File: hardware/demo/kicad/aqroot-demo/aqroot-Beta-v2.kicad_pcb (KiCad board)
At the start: 6 copper layers, 72 x 148 mm, 311 parts, among them J1 FH69-50S-0.5SH, J2 Molex_5025700893, J3 USB_C_Receptacle_USB2.0_16P, J4 JST-PH-2 BATTERY, J5 COMMUNITY_PORT_1x24, J6 JST-PH-2 SPEAKER, J7 BM02B-ACHSS-GAN-ETF, J8 QWIIC_STEMMA_QT, Q1 AO3400A, Q10 2N7002, Q2 NTMD4820N, Q3 NTMD4820N, Q4 BSS138, Q5 AO3401A, Q6 BSS138, Q7 BSS138, Q8 BSS138, Q9 BSS138, SW1 BOOT, SW2 UP, SW3 DOWN, SW4 LEFT, SW5 RIGHT, SW6 A_SELECT, SW7 B_BACK, SW9 SW_SPDT, U1 ESP32-S3-WROOM-1, U10 USBLC6-2SC6, U11 BQ25185, U12 TPS63020, U13 TPS61023, U14 MAX17048, U16 TCA4307DGKR, U17 TPS61169DCKR, U18 LTC4368-1, U19 TLV7032, U2 PCAL9535APW, U20 TPS22950C, U21 TPS61023, U22 TPS22950C, U3 PCAL9535APW, U4 BMI270, U5 MAX98357A, U6 TSOP38238, U7 E07-400M10S, U8 E22-900M22S, U9 ST25R3916-AQET, Y1 27.12MHz 10pF 3225-4P

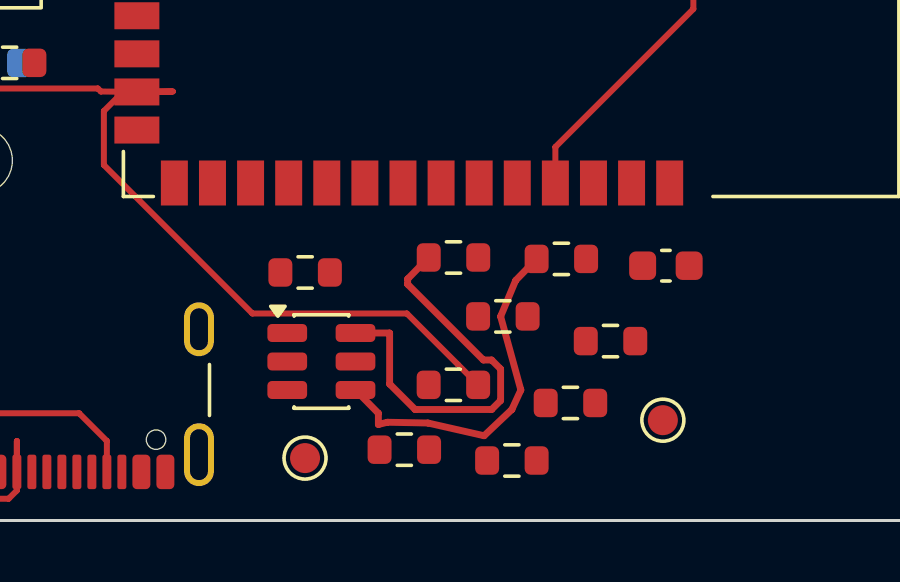
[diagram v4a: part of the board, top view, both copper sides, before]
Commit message: demo: route native A internal leg
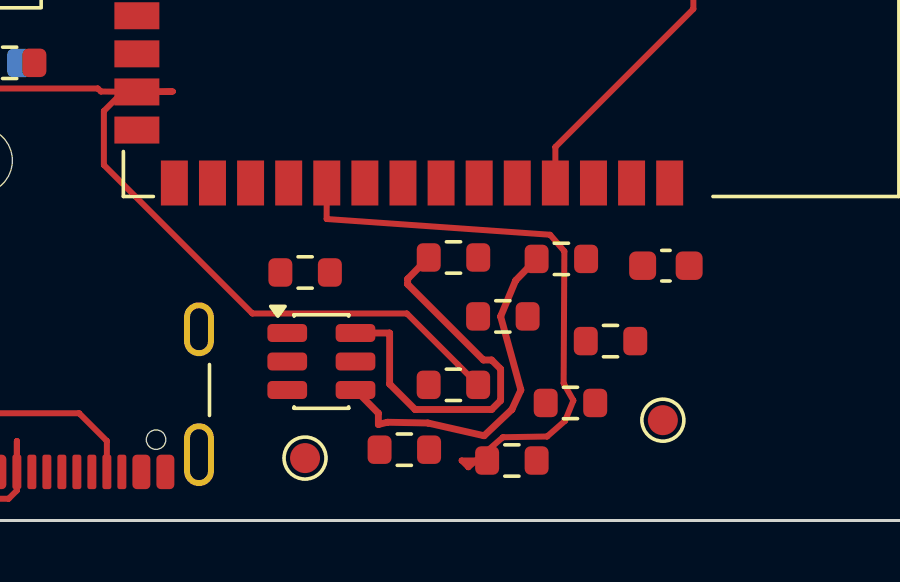
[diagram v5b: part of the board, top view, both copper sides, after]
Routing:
- net /NATIVE_A: track 0.00 -> 20.1 mm
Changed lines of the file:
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@@
+	)
+	(segment
+		(start 59.8 144)
+		(end 59.525 144.675)
+		(width 0.2)
+		(layer "F.Cu")
+		(net "/NATIVE_A")
+	)
+	(segment
+		(start 59.5 139.025)
+		(end 59.475 143.425)
+		(width 0.2)
+		(layer "F.Cu")
+		(net "/NATIVE_A")
+	)
+	(segment
+		(start 59.525 144.675)
+		(end 58.925 145.2)
+		(width 0.2)
+		(layer "F.Cu")
+		(net "/NATIVE_A")
+	)
+	(segment
+		(start 51.58 136.75)
+		(end 51.575 137.95)
+		(width 0.2)
+		(layer "F.Cu")
+		(net "/NATIVE_A")
+	)
+	(segment
+		(start 57.45 145.225)
+		(end 56.3 146.225)
+		(width 0.2)
+		(layer "F.Cu")
+		(net "/NATIVE_A")
+	)
+	(segment
+		(start 58.925 145.2)
+		(end 57.45 145.225)
+		(width 0.2)
+		(layer "F.Cu")
+		(net "/NATIVE_A")
+	)
+	(segment
+		(start 59.025 138.475)
+		(end 59.5 139.025)
+		(width 0.2)
+		(layer "F.Cu")
+		(net "/NATIVE_A")
+	)
+	(segment
+		(start 51.575 137.95)
+		(end 59.025 138.475)
+		(width 0.2)
+		(layer "F.Cu")
+		(net "/NATIVE_A")
+	)
+	(segment
+		(start 56.925 146)
+		(end 56.075 146)
+		(width 0.2)
+		(layer "F.Cu")
+		(net "/NATIVE_A")
+	)
+	(segment
+		(start 59.475 143.425)
+		(end 59.8 144)
+		(width 0.2)
+		(layer "F.Cu")
+		(net "/NATIVE_A")
+	)
+	(segment
+		(start 56.3 146.225)
+		(end 56.075 146)
+		(width 0.2)
+		(layer "F.Cu")
+		(net "/NATIVE_A")
 	)
 	(segment

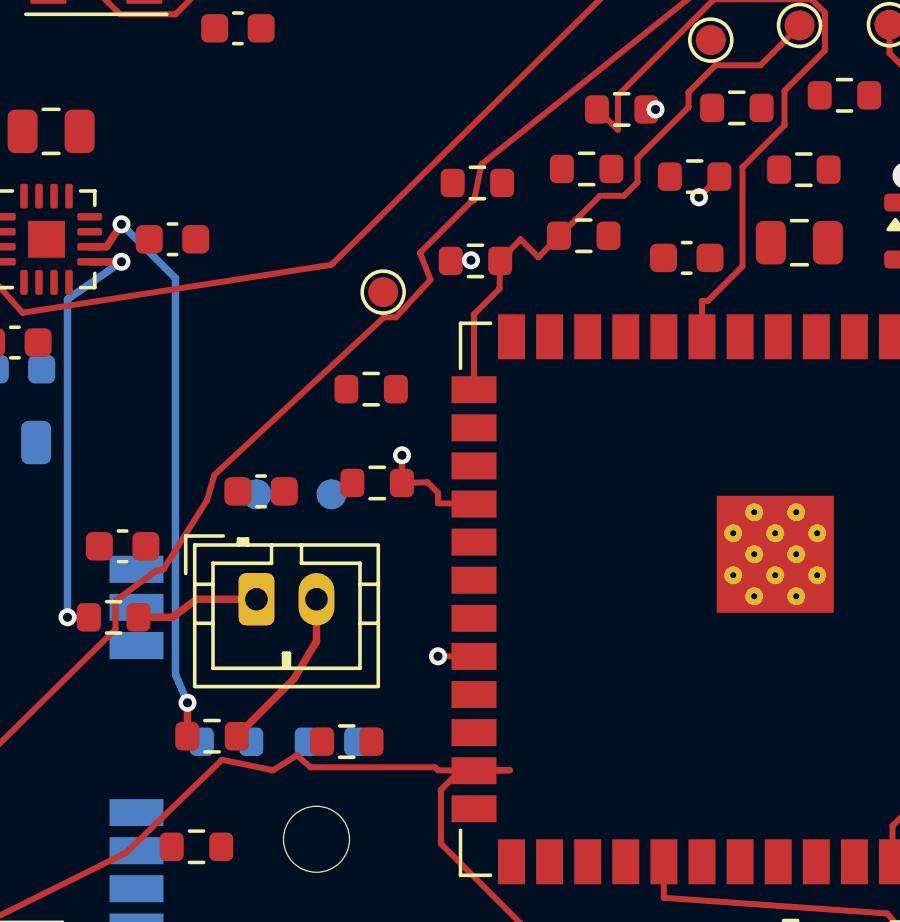
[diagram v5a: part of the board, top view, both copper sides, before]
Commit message: demo: route native B internal leg
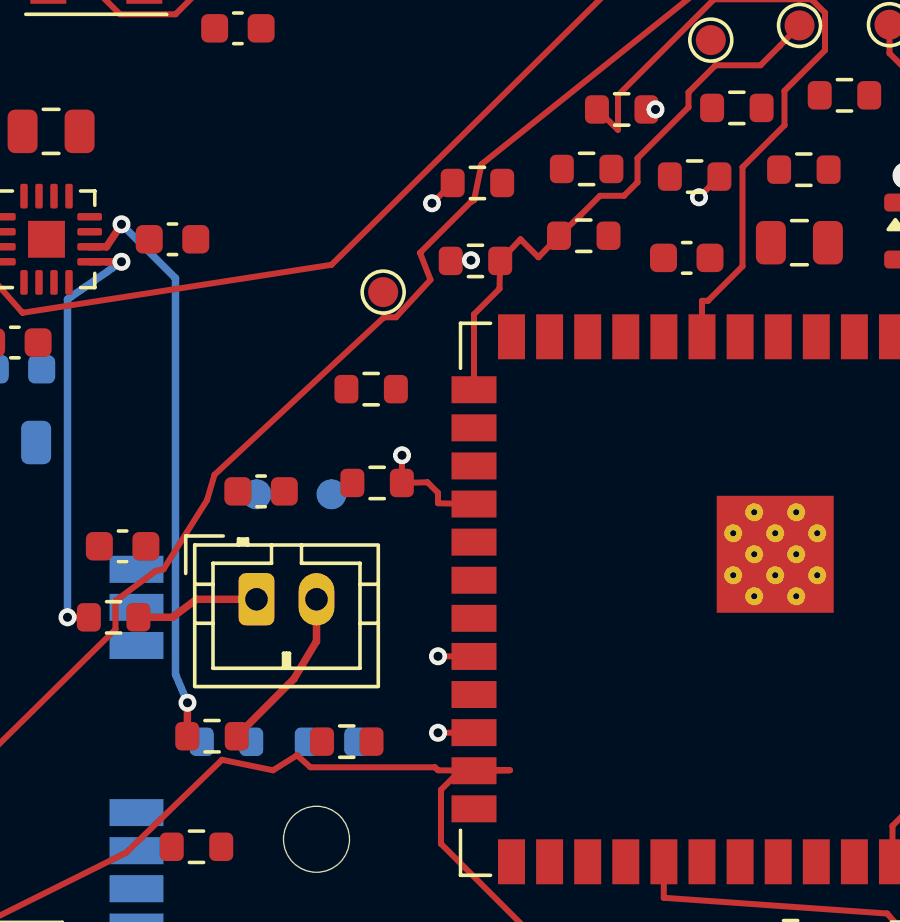
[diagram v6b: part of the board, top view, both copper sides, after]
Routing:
- net /NATIVE_B: track 0.00 -> 20.4 mm, vias 0 -> 2
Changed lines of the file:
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@@
+	)
+	(segment
+		(start 44.538976 114.123889)
+		(end 43.85 114.8)
+		(width 0.2)
+		(layer "F.Cu")
+		(net "/NATIVE_B")
+	)
+	(segment
+		(start 45.25 132.445)
+		(end 44.05 132.45)
+		(width 0.2)
+		(layer "F.Cu")
+		(net "/NATIVE_B")
+	)
+	(via
+		(at 44.05 132.45)
+		(size 0.6)
+		(drill 0.3)
+		(layers "F.Cu" "B.Cu")
+		(net "/NATIVE_B")
+	)
+	(via
+		(at 43.85 114.8)
+		(size 0.6)
+		(drill 0.3)
+		(layers "F.Cu" "B.Cu")
+		(net "/NATIVE_B")
+	)
+	(segment
+		(start 43.85 116.4)
+		(end 43.85 114.8)
+		(width 0.2)
+		(layer "In2.Cu")
+		(net "/NATIVE_B")
+	)
+	(segment
+		(start 44.05 132.45)
+		(end 44.7 131.8)
+		(width 0.2)
+		(layer "In2.Cu")
+		(net "/NATIVE_B")
+	)
+	(segment
+		(start 44.7 117.25)
+		(end 43.85 116.4)
+		(width 0.2)
+		(layer "In2.Cu")
+		(net "/NATIVE_B")
+	)
+	(segment
+		(start 44.7 131.8)
+		(end 44.7 117.25)
+		(width 0.2)
+		(layer "In2.Cu")
+		(net "/NATIVE_B")
 	)
 	(segment

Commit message: demo: route SPI-A MISO
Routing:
- net /SPI_A_MISO: track 0.00 -> 28.7 mm, vias 0 -> 2
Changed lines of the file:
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@@
+	)
+	(segment
+		(start 44.05 128.65)
+		(end 43.3 128.65)
+		(width 0.2)
+		(layer "F.Cu")
+		(net "/SPI_A_MISO")
+	)
+	(segment
+		(start 45.25 128.635)
+		(end 44.05 128.65)
+		(width 0.2)
+		(layer "F.Cu")
+		(net "/SPI_A_MISO")
+	)
+	(segment
+		(start 18.794 132.462)
+		(end 18.8 131.25)
+		(width 0.2)
+		(layer "F.Cu")
+		(net "/SPI_A_MISO")
+	)
+	(via
+		(at 43.3 128.65)
+		(size 0.6)
+		(drill 0.3)
+		(layers "F.Cu" "B.Cu")
+		(net "/SPI_A_MISO")
+	)
+	(via
+		(at 18.8 131.25)
+		(size 0.6)
+		(drill 0.3)
+		(layers "F.Cu" "B.Cu")
+		(net "/SPI_A_MISO")
+	)
+	(segment
+		(start 19.25 130.8)
+		(end 18.8 131.25)
+		(width 0.2)
+		(layer "In2.Cu")
+		(net "/SPI_A_MISO")
+	)
+	(segment
+		(start 41.15 130.8)
+		(end 19.25 130.8)
+		(width 0.2)
+		(layer "In2.Cu")
+		(net "/SPI_A_MISO")
+	)
+	(segment
+		(start 43.3 128.65)
+		(end 41.15 130.8)
+		(width 0.2)
+		(layer "In2.Cu")
+		(net "/SPI_A_MISO")
 	)
 	(segment

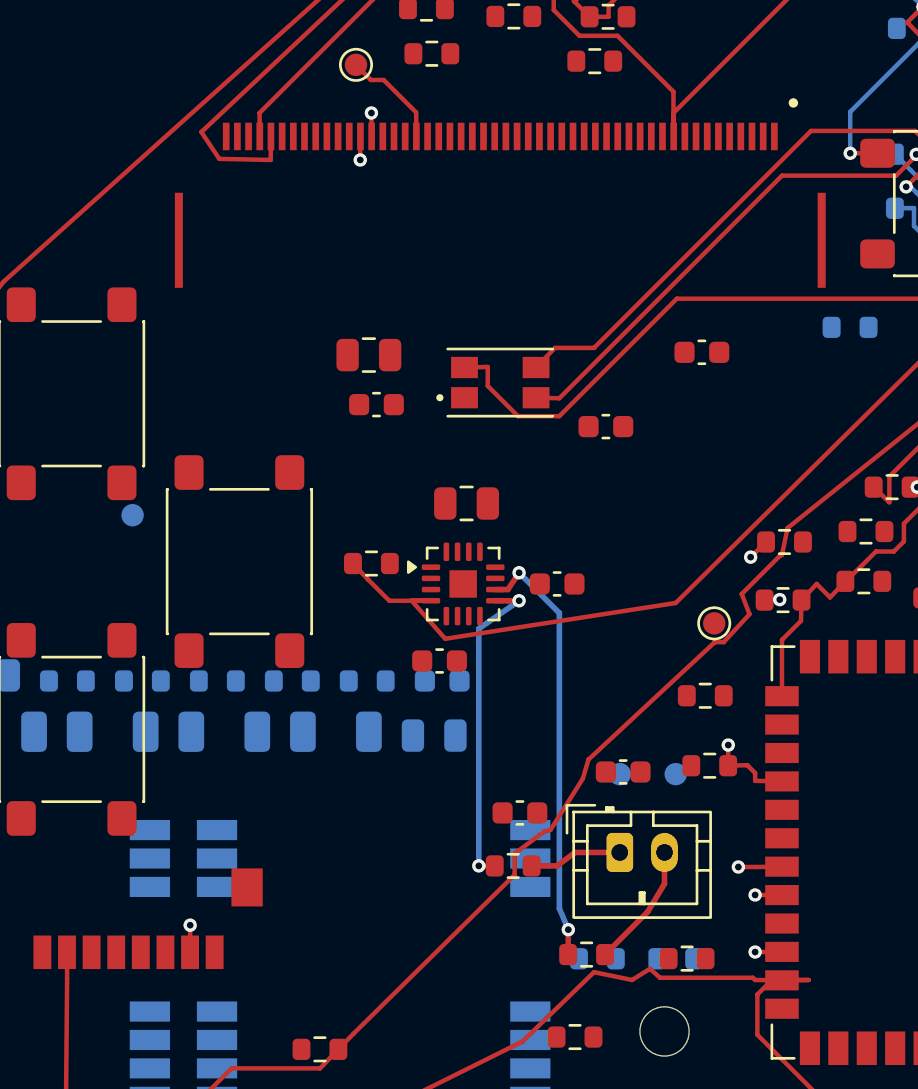
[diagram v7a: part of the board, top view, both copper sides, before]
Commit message: demo: route SPI-A clock tree
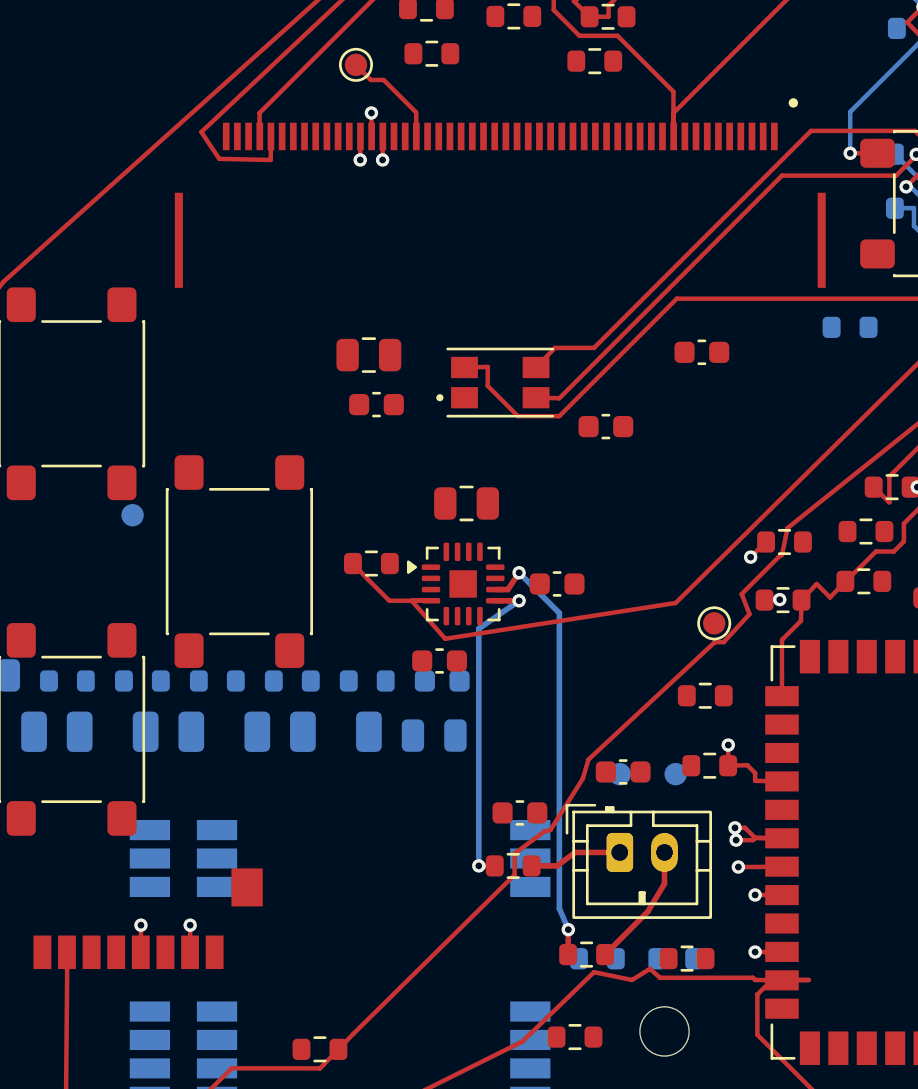
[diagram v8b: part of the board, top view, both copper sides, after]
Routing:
- net /SPI_A_SCK: track 0.00 -> 72.8 mm, vias 0 -> 4
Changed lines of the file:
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@@
+	)
+	(segment
+		(start 45.25 127.365)
+		(end 44.05 127.35)
+		(width 0.2)
+		(layer "F.Cu")
+		(net "/SPI_A_SCK")
+	)
+	(segment
+		(start 43.6 126.9)
+		(end 43.15 126.9)
+		(width 0.2)
+		(layer "F.Cu")
+		(net "/SPI_A_SCK")
+	)
+	(segment
+		(start 16.594 132.462)
+		(end 16.6 131.25)
+		(width 0.2)
+		(layer "F.Cu")
+		(net "/SPI_A_SCK")
+	)
+	(segment
+		(start 43.95 127.45)
+		(end 43.2 127.45)
+		(width 0.2)
+		(layer "F.Cu")
+		(net "/SPI_A_SCK")
+	)
+	(segment
+		(start 44.05 127.35)
+		(end 43.6 126.9)
+		(width 0.2)
+		(layer "F.Cu")
+		(net "/SPI_A_SCK")
+	)
+	(segment
+		(start 27.41 96)
+		(end 27.4 97.05)
+		(width 0.2)
+		(layer "F.Cu")
+		(net "/SPI_A_SCK")
+	)
+	(segment
+		(start 45.25 127.365)
+		(end 44.05 127.35)
+		(width 0.2)
+		(layer "F.Cu")
+		(net "/SPI_A_SCK")
+	)
+	(segment
+		(start 44.05 127.35)
+		(end 43.95 127.45)
+		(width 0.2)
+		(layer "F.Cu")
+		(net "/SPI_A_SCK")
+	)
+	(via
+		(at 27.4 97.05)
+		(size 0.6)
+		(drill 0.3)
+		(layers "F.Cu" "B.Cu")
+		(net "/SPI_A_SCK")
+	)
+	(via
+		(at 43.15 126.9)
+		(size 0.6)
+		(drill 0.3)
+		(layers "F.Cu" "B.Cu")
+		(net "/SPI_A_SCK")
+	)
+	(via
+		(at 16.6 131.25)
+		(size 0.6)
+		(drill 0.3)
+		(layers "F.Cu" "B.Cu")
+		(net "/SPI_A_SCK")
+	)
+	(via
+		(at 43.2 127.45)
+		(size 0.6)
+		(drill 0.3)
+		(layers "F.Cu" "B.Cu")
+		(net "/SPI_A_SCK")
+	)
+	(segment
+		(start 17.5 130.35)
+		(end 16.6 131.25)
+		(width 0.2)
+		(layer "In2.Cu")
+		(net "/SPI_A_SCK")
+	)
+	(segment
+		(start 43.2 127.45)
+		(end 25.6 96.95)
+		(width 0.2)
+		(layer "In2.Cu")
+		(net "/SPI_A_SCK")
+	)
+	(segment
+		(start 43.15 126.9)
+		(end 39.7 130.35)
+		(width 0.2)
+		(layer "In2.Cu")
+		(net "/SPI_A_SCK")
+	)
+	(segment
+		(start 39.7 130.35)
+		(end 17.5 130.35)
+		(width 0.2)
+		(layer "In2.Cu")
+		(net "/SPI_A_SCK")
+	)
+	(segment
+		(start 26.45 96.1)
+		(end 27.4 97.05)
+		(width 0.2)
+		(layer "In2.Cu")
+		(net "/SPI_A_SCK")
+	)
+	(segment
+		(start 25.6 96.95)
+		(end 26.45 96.1)
+		(width 0.2)
+		(layer "In2.Cu")
+		(net "/SPI_A_SCK")
 	)
 	(segment
